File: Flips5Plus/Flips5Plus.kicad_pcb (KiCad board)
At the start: 2 copper layers, 80 x 75 mm, 11 parts, among them CN1 Conn_02x30_Odd_Even, CN2 UFP2810, CN3 UFP2810, U1 FP2800A, U2 FP2800A

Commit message: toggling copper behind "K" of "KiCad" logo
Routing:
- added copper zone on F.Cu, net (none)
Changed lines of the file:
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@@
+    )
+  )
+  (zone (net 0) (net_name "") (layer F.Cu) (hatch edge 0.508)
+    (connect_pads (clearance 0.23))
+    (min_thickness 0.254)
+    (fill yes (arc_segments 16) (thermal_gap 0.508) (thermal_bridge_width 0.508))
+    (polygon
+      (pts
+        (xy 142 109.4) (xy 142.35 109.45) (xy 145.55 109.45) (xy 145.55 112.45) (xy 142 112.45)
+      )
     )
   )

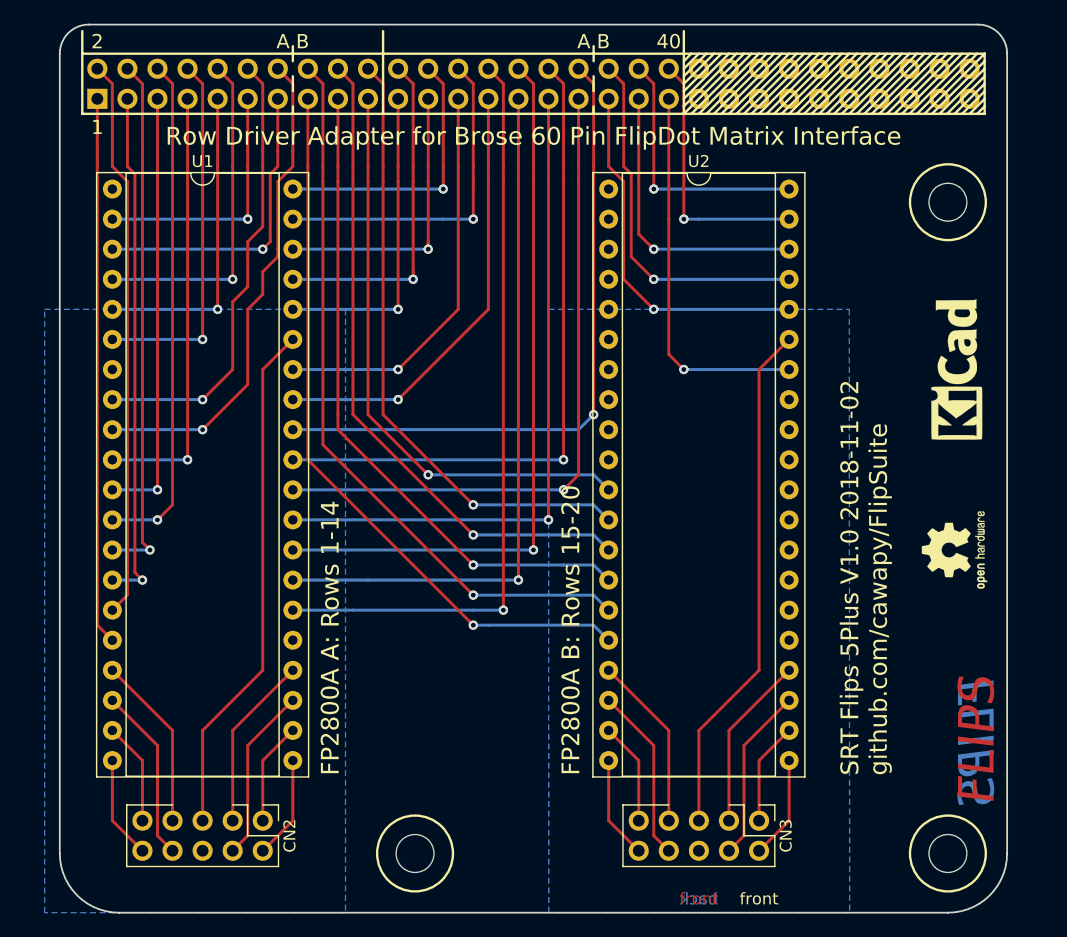
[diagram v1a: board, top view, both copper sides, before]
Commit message: set flip current traces to 0.5mm
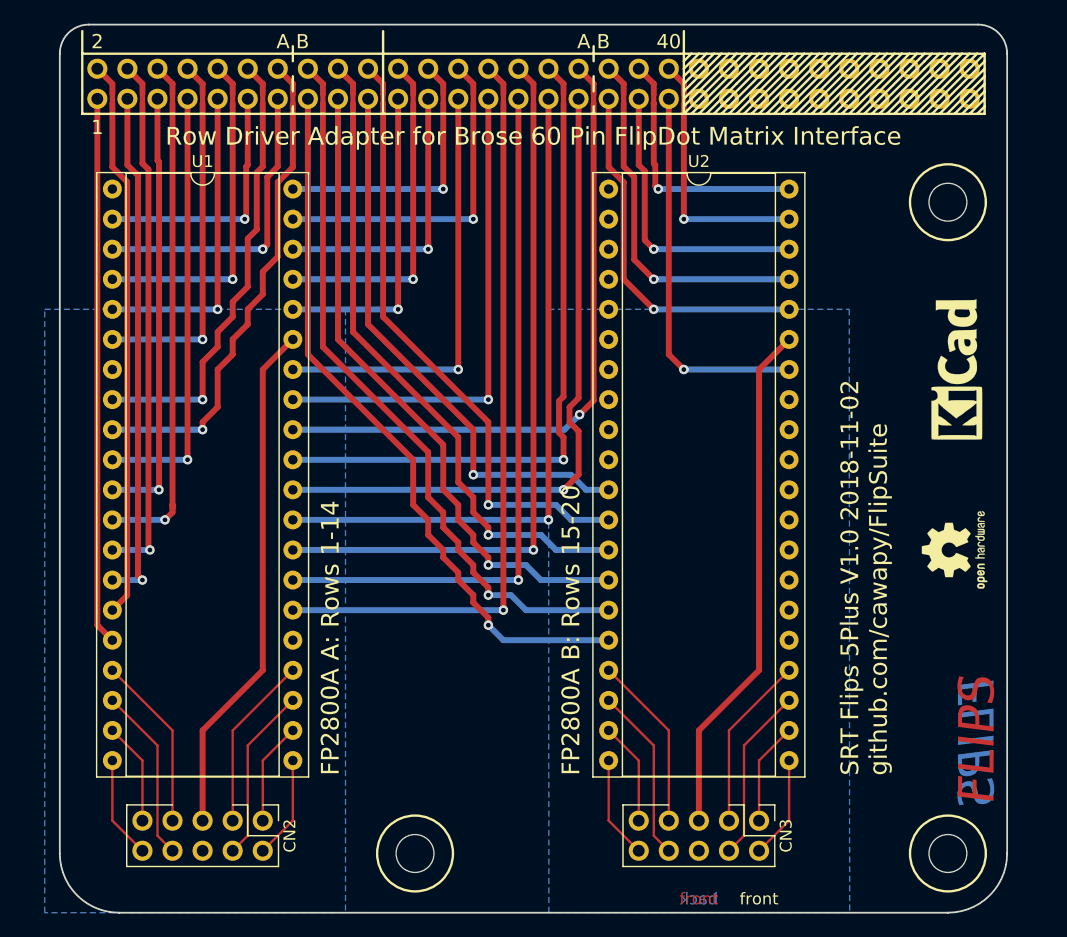
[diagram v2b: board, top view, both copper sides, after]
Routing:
- net Net-(CN1-Pad27): track 37.4 -> 41.9 mm
- net Net-(CN1-Pad25): track 33.9 -> 36.8 mm
- net Net-(CN1-Pad19): track 49.6 -> 47.4 mm
- net Net-(CN1-Pad17): track 56.1 -> 55.3 mm
- net Net-(CN1-Pad18): track 56.1 -> 55.3 mm
- net Net-(CN1-Pad16): track 62.2 -> 61.4 mm
- net Net-(CN1-Pad20): track 52.5 -> 51.7 mm
- net Net-(CN1-Pad15): track 62.2 -> 61.4 mm
- net Net-(CN1-Pad6): track 43.0 -> 43.7 mm
- net Net-(CN1-Pad34): track 55.7 -> 55.0 mm
- net Net-(CN1-Pad33): track 56.4 -> 57.0 mm
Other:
- net class Default: trace_width 0.25 -> 0.2
- net class POW added: clearance 0.2, trace_width 0.5, via_dia 0.8, via_drill 0.4

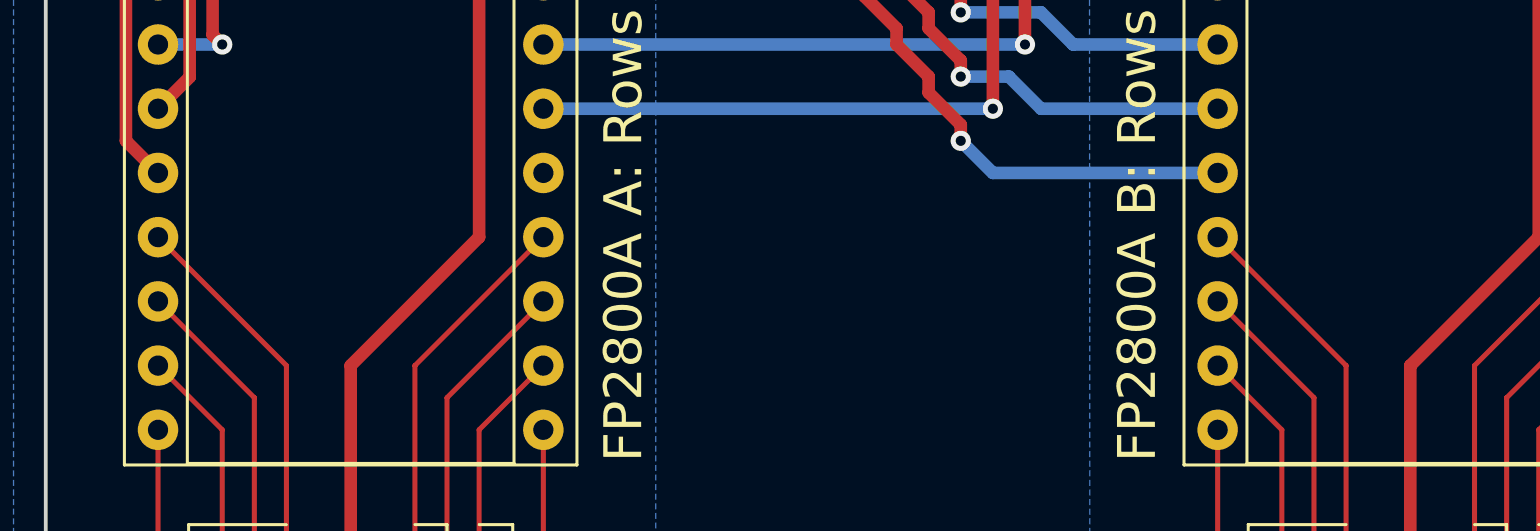
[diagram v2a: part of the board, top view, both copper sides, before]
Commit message: adding bypass capacitors
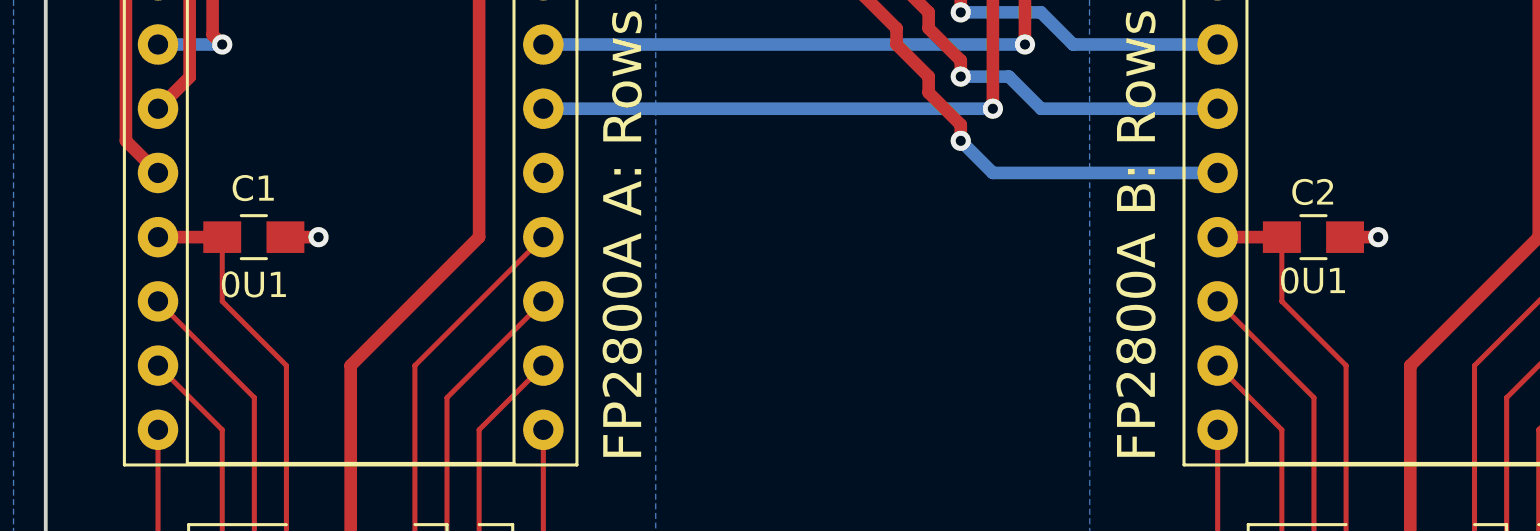
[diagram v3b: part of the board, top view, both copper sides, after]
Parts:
- added C1: 0U1, Capacitors_SMD:C_0805_HandSoldering, F.Cu at (76.2, 132.1)
- added C2: 0U1, Capacitors_SMD:C_0805_HandSoldering, F.Cu at (118.1, 132.1)
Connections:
- CN1 pad 41: (no net) -> Net-(CN1-Pad41)
- CN1 pad 42: (no net) -> Net-(CN1-Pad42)
- CN1 pad 43: (no net) -> Net-(CN1-Pad43)
- CN1 pad 44: (no net) -> Net-(CN1-Pad44)
- CN1 pad 45: (no net) -> Net-(CN1-Pad45)
- CN1 pad 46: (no net) -> Net-(CN1-Pad46)
- CN1 pad 47: (no net) -> Net-(CN1-Pad47)
- CN1 pad 48: (no net) -> Net-(CN1-Pad48)
- CN1 pad 49: (no net) -> Net-(CN1-Pad49)
- CN1 pad 50: (no net) -> Net-(CN1-Pad50)
- CN1 pad 51: (no net) -> Net-(CN1-Pad51)
- CN1 pad 52: (no net) -> Net-(CN1-Pad52)
- CN1 pad 53: (no net) -> Net-(CN1-Pad53)
- CN1 pad 54: (no net) -> Net-(CN1-Pad54)
- CN1 pad 55: (no net) -> Net-(CN1-Pad55)
- CN1 pad 56: (no net) -> Net-(CN1-Pad56)
- CN1 pad 57: (no net) -> Net-(CN1-Pad57)
- CN1 pad 58: (no net) -> Net-(CN1-Pad58)
- CN1 pad 59: (no net) -> Net-(CN1-Pad59)
- CN1 pad 60: (no net) -> Net-(CN1-Pad60)
- U1 pad 1: (no net) -> Net-(U1-Pad1)
- U2 pad 1: (no net) -> Net-(U2-Pad1)
- U2 pad 10: (no net) -> Net-(U2-Pad10)
- U2 pad 2: (no net) -> Net-(U2-Pad2)
- U2 pad 26: (no net) -> Net-(U2-Pad26)
- U2 pad 27: (no net) -> Net-(U2-Pad27)
- U2 pad 28: (no net) -> Net-(U2-Pad28)
- U2 pad 29: (no net) -> Net-(U2-Pad29)
- U2 pad 3: (no net) -> Net-(U2-Pad3)
- U2 pad 30: (no net) -> Net-(U2-Pad30)
- U2 pad 31: (no net) -> Net-(U2-Pad31)
- U2 pad 32: (no net) -> Net-(U2-Pad32)
- U2 pad 33: (no net) -> Net-(U2-Pad33)
- U2 pad 4: (no net) -> Net-(U2-Pad4)
- U2 pad 5: (no net) -> Net-(U2-Pad5)
- U2 pad 6: (no net) -> Net-(U2-Pad6)
- U2 pad 8: (no net) -> Net-(U2-Pad8)
- U2 pad 9: (no net) -> Net-(U2-Pad9)
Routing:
- net /R.VCC: track 14.8 -> 16.3 mm
- net /L.VCC: track 14.8 -> 16.3 mm
- net /R.GND: track 0.00 -> 1.31 mm, vias 0 -> 1
- net /L.GND: track 0.00 -> 1.31 mm, vias 0 -> 1
